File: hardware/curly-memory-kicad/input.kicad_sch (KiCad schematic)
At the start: 28 parts, among them J201 AudioJack2, J202 AudioJack2, J203 AudioJack2, J204 Conn_01x01_Male, J205 Conn_01x01_Male, J206 Conn_01x01_Male, J207 Conn_01x01_Male, U201 MCP6004

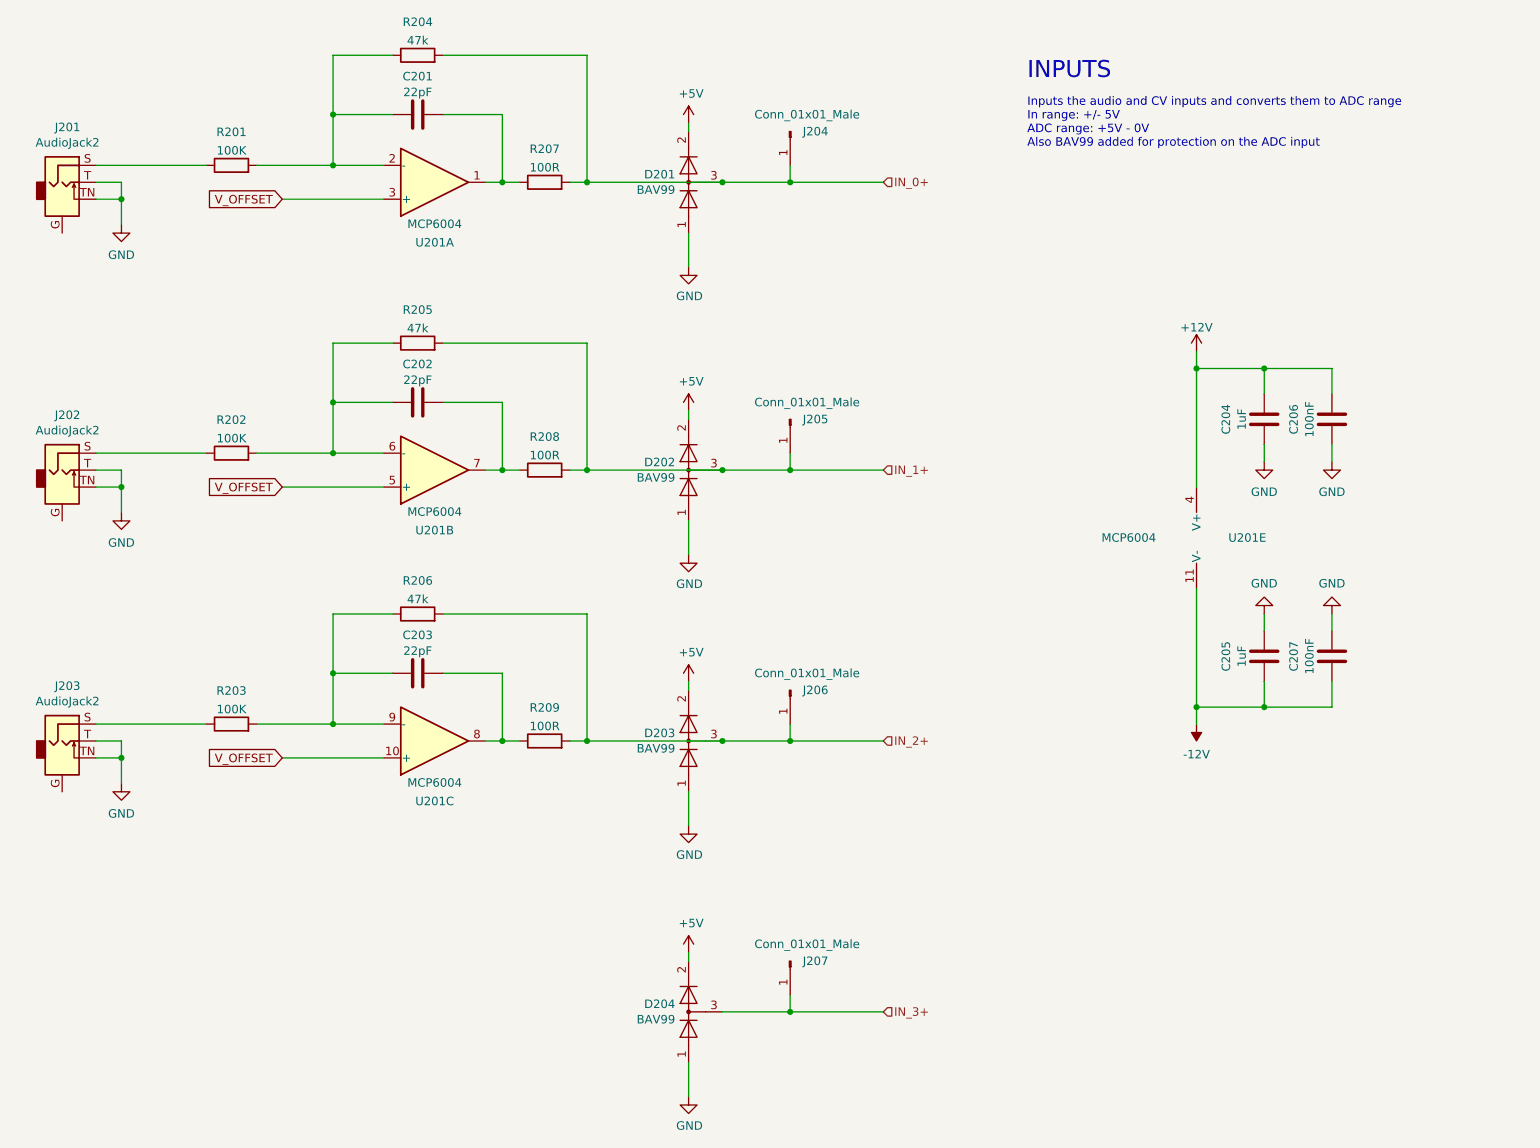
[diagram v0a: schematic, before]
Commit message: all components placed on the main board
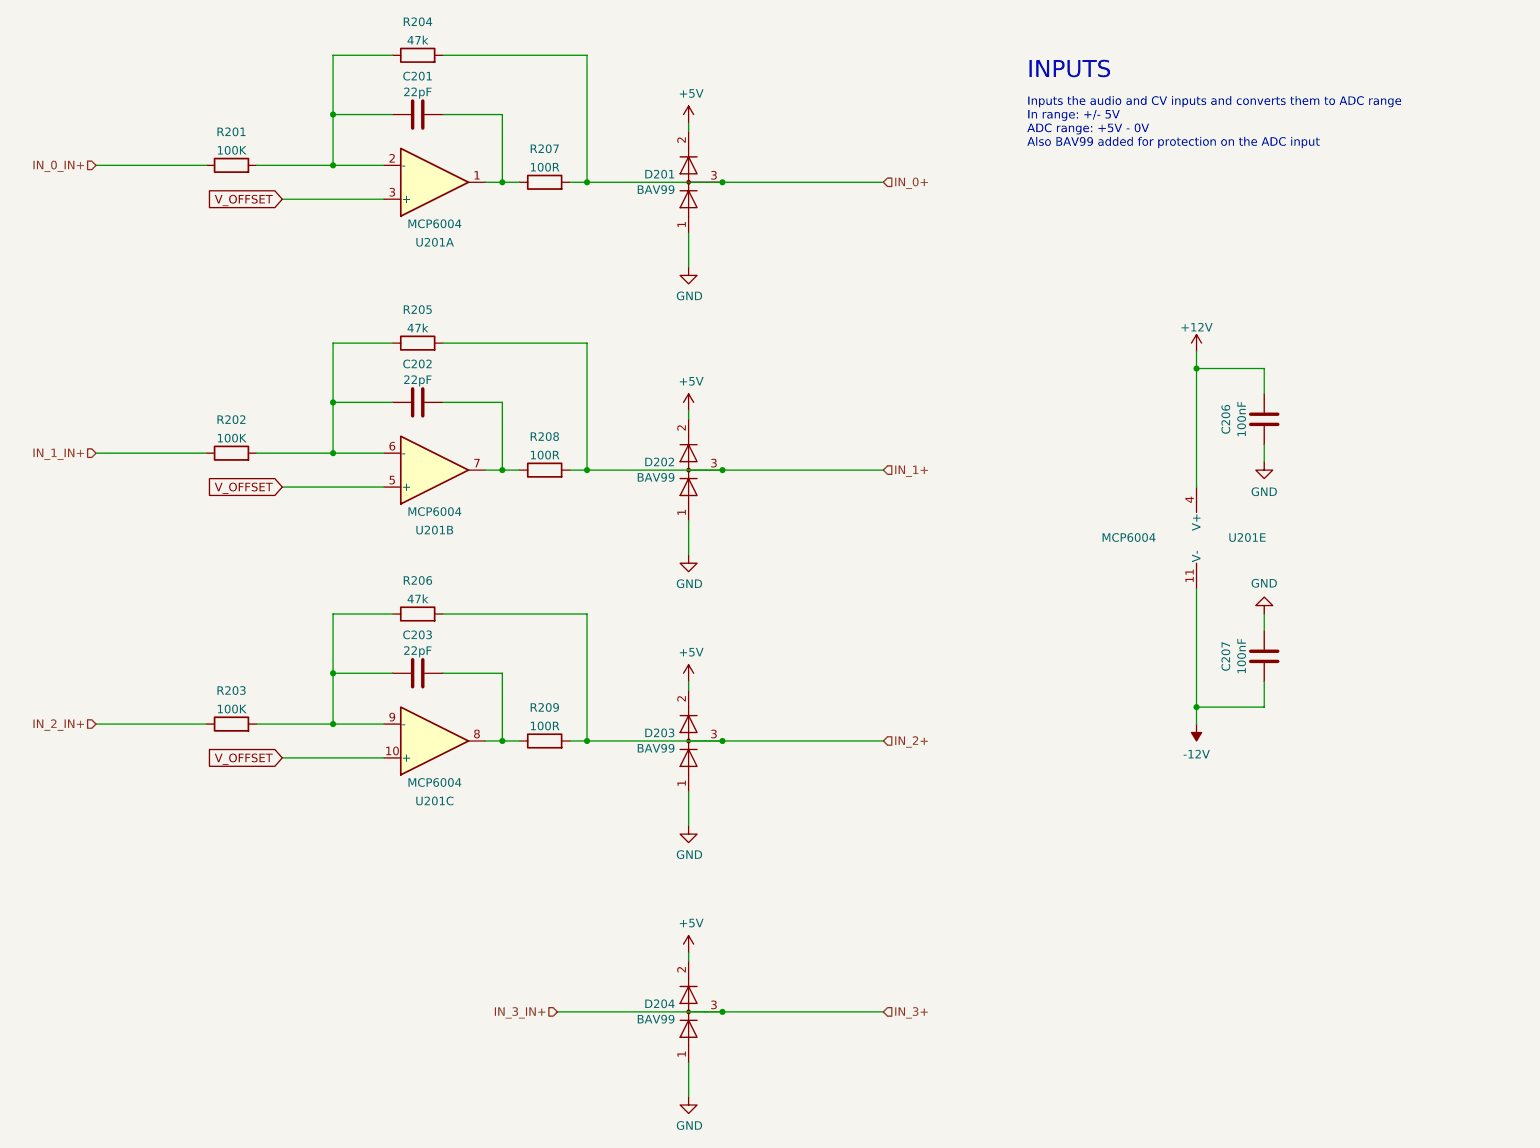
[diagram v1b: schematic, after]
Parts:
- removed C204, C205: 1uF, Capacitor_SMD:C_0805_2012Metric_Pad1.18x1.45mm_HandSolder, symbol Device:C
- removed J201, J202, J203: AudioJack2, AudioJacks:Jack_3.5mm_QingPu_WQP-PJ398SM_Vertical, symbol Connector:AudioJack2_Ground_SwitchT
- removed J204, J205, J206, J207: Conn_01x01_Male, Connector_PinSocket_2.54mm:PinSocket_1x01_P2.54mm_Vertical, symbol Connector:Conn_01x01_Male
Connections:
- net IN_0_IN+: now reaches R201.1
- net IN_1_IN+: now reaches R202.1
- net IN_2_IN+: now reaches R203.1
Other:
- moved on the sheet: C206, C207

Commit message: gerbers genearted and mf/mfpn added for main board for build
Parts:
- C201, C202, C203: MF (none) -> Samsung; MFPN (none) -> CL21C220JBANNNC; Material (none) -> CG0 / NP0; Voltage (none) -> 50V
- C206, C207: MF (none) -> Samsung; MFPN (none) -> CL21B104KBCNNNC; Material (none) -> X7R; Voltage (none) -> 50V
- R201, R202, R203: MF (none) -> Multicomp; MFPN (none) -> MCWR08X1003FTL; Tolerance (none) -> 1%
- R204, R205, R206: value 47k -> 47K; MF (none) -> Multicomp; MFPN (none) -> MCWR08X4702FTL; Tolerance (none) -> 1%
- R207, R208, R209: MF (none) -> Multicomp; MFPN (none) -> MCWR08X1000FTL; Tolerance (none) -> 1%
- U201: value MCP6004 -> MCP6004-I/SL
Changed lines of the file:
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@@
     (in_bom yes) (on_board yes) (fields_autoplaced)
     (property "Reference" "R206" (id 0) (at 81.28 100.4275 90))
-    (property "Value" "47k" (id 1) (at 81.28 103.2026 90))
+    (property "Value" "47K" (id 1) (at 81.28 103.2026 90))
     (property "Footprint" "Resistor_SMD:R_0805_2012Metric_Pad1.20x1.40mm_HandSolder" (id 2) (at 81.28 107.188 90)
       (effects (font (size 1.27 1.27)) hide)
     )
     (property "Datasheet" "~" (id 3) (at 81.28 105.41 0)
+      (effects (font (size 1.27 1.27)) hide)
+    )
+    (property "MF" "Multicomp" (id 4) (at 81.28 105.41 0)
+      (effects (font (size 1.27 1.27)) hide)
+    )
+    (property "MFPN" "MCWR08X4702FTL " (id 5) (at 81.28 105.41 0)
+      (effects (font (size 1.27 1.27)) hide)
+    )
+    (property "Tolerance" "1%" (id 6) (at 81.28 105.41 0)
       (effects (font (size 1.27 1.27)) hide)
     )
@@
       (effects (font (size 1.27 1.27)) hide)
     )
+    (property "Voltage" "50V" (id 4) (at 81.28 30.48 0)
+      (effects (font (size 1.27 1.27)) hide)
+    )
+    (property "MF" "Samsung" (id 5) (at 81.28 30.48 0)
+      (effects (font (size 1.27 1.27)) hide)
+    )
+    (property "MFPN" "CL21C220JBANNNC" (id 6) (at 81.28 30.48 0)
+      (effects (font (size 1.27 1.27)) hide)
+    )
+    (property "Material" "CG0 / NP0" (id 7) (at 81.28 30.48 0)
+      (effects (font (size 1.27 1.27)) hide)
+    )
     (pin "1")
     (pin "2")
@@
     (in_bom yes) (on_board yes) (fields_autoplaced)
     (property "Reference" "U201" (id 0) (at 83.82 49.6865 0))
-    (property "Value" "MCP6004" (id 1) (at 83.82 46.9114 0))
+    (property "Value" "MCP6004-I/SL" (id 1) (at 83.82 46.9114 0))
     (property "Footprint" "Package_SO:SOIC-14_3.9x8.7mm_P1.27mm" (id 2) (at 82.55 43.18 0)
       (effects (font (size 1.27 1.27)) hide)
@@
     (in_bom yes) (on_board yes) (fields_autoplaced)
     (property "Reference" "R205" (id 0) (at 81.28 59.7875 90))
-    (property "Value" "47k" (id 1) (at 81.28 62.5626 90))
+    (property "Value" "47K" (id 1) (at 81.28 62.5626 90))
     (property "Footprint" "Resistor_SMD:R_0805_2012Metric_Pad1.20x1.40mm_HandSolder" (id 2) (at 81.28 66.548 90)
       (effects (font (size 1.27 1.27)) hide)
     )
     (property "Datasheet" "~" (id 3) (at 81.28 64.77 0)
+      (effects (font (size 1.27 1.27)) hide)
+    )
+    (property "MF" "Multicomp" (id 4) (at 81.28 64.77 0)
+      (effects (font (size 1.27 1.27)) hide)
+    )
+    (property "MFPN" "MCWR08X4702FTL " (id 5) (at 81.28 64.77 0)
+      (effects (font (size 1.27 1.27)) hide)
+    )
+    (property "Tolerance" "1%" (id 6) (at 81.28 64.77 0)
       (effects (font (size 1.27 1.27)) hide)
     )
@@
       (effects (font (size 1.27 1.27)) hide)
     )
+    (property "Voltage" "50V" (id 4) (at 81.28 73.66 0)
+      (effects (font (size 1.27 1.27)) hide)
+    )
+    (property "MF" "Samsung" (id 5) (at 81.28 73.66 0)
+      (effects (font (size 1.27 1.27)) hide)
+    )
+    (property "MFPN" "CL21C220JBANNNC" (id 6) (at 81.28 73.66 0)
+      (effects (font (size 1.27 1.27)) hide)
+    )
+    (property "Material" "CG0 / NP0" (id 7) (at 81.28 73.66 0)
+      (effects (font (size 1.27 1.27)) hide)
+    )
     (pin "1")
     (pin "2")
@@
       (effects (font (size 1.27 1.27)) hide)
     )
+    (property "Voltage" "50V" (id 4) (at 208.28 111.76 0)
+      (effects (font (size 1.27 1.27)) hide)
+    )
+    (property "MF" "Samsung" (id 5) (at 208.28 111.76 0)
+      (effects (font (size 1.27 1.27)) hide)
+    )
+    (property "MFPN" "CL21B104KBCNNNC" (id 6) (at 208.28 111.76 0)
+      (effects (font (size 1.27 1.27)) hide)
+    )
+    (property "Material" "X7R" (id 7) (at 208.28 111.76 0)
+      (effects (font (size 1.27 1.27)) hide)
+    )
     (pin "1")
     (pin "2")
@@
       (effects (font (size 1.27 1.27)) hide)
     )
+    (property "MF" "Multicomp" (id 4) (at 100.33 124.46 0)
+      (effects (font (size 1.27 1.27)) hide)
+    )
+    (property "MFPN" "MCWR08X1000FTL " (id 5) (at 100.33 124.46 0)
+      (effects (font (size 1.27 1.27)) hide)
+    )
+    (property "Tolerance" "1%" (id 6) (at 100.33 124.46 0)
+      (effects (font (size 1.27 1.27)) hide)
+    )
     (pin "1")
     (pin "2")
@@
       (effects (font (size 1.27 1.27)) hide)
     )
+    (property "Voltage" "50V" (id 4) (at 81.28 114.3 0)
+      (effects (font (size 1.27 1.27)) hide)
+    )
+    (property "MF" "Samsung" (id 5) (at 81.28 114.3 0)
+      (effects (font (size 1.27 1.27)) hide)
+    )
+    (property "MFPN" "CL21C220JBANNNC" (id 6) (at 81.28 114.3 0)
+      (effects (font (size 1.27 1.27)) hide)
+    )
+    (property "Material" "CG0 / NP0" (id 7) (at 81.28 114.3 0)
+      (effects (font (size 1.27 1.27)) hide)
+    )
     (pin "1")
     (pin "2")
@@
       (effects (font (size 1.27 1.27)) hide)
     )
+    (property "MF" "Multicomp" (id 4) (at 100.33 40.64 0)
+      (effects (font (size 1.27 1.27)) hide)
+    )
+    (property "MFPN" "MCWR08X1000FTL " (id 5) (at 100.33 40.64 0)
+      (effects (font (size 1.27 1.27)) hide)
+    )
+    (property "Tolerance" "1%" (id 6) (at 100.33 40.64 0)
+      (effects (font (size 1.27 1.27)) hide)
+    )
     (pin "1")
     (pin "2")
@@
       (effects (font (size 1.27 1.27)) hide)
     )
+    (property "Voltage" "50V" (id 4) (at 208.28 76.2 0)
+      (effects (font (size 1.27 1.27)) hide)
+    )
+    (property "MF" "Samsung" (id 5) (at 208.28 76.2 0)
+      (effects (font (size 1.27 1.27)) hide)
+    )
+    (property "MFPN" "CL21B104KBCNNNC" (id 6) (at 208.28 76.2 0)
+      (effects (font (size 1.27 1.27)) hide)
+    )
+    (property "Material" "X7R" (id 7) (at 208.28 76.2 0)
+      (effects (font (size 1.27 1.27)) hide)
+    )
     (pin "1")
     (pin "2")
@@
     (in_bom yes) (on_board yes) (fields_autoplaced)
     (property "Reference" "R204" (id 0) (at 81.28 16.6075 90))
-    (property "Value" "47k" (id 1) (at 81.28 19.3826 90))
+    (property "Value" "47K" (id 1) (at 81.28 19.3826 90))
     (property "Footprint" "Resistor_SMD:R_0805_2012Metric_Pad1.20x1.40mm_HandSolder" (id 2) (at 81.28 23.368 90)
       (effects (font (size 1.27 1.27)) hide)
@@
       (effects (font (size 1.27 1.27)) hide)
     )
+    (property "MF" "Multicomp" (id 4) (at 81.28 21.59 0)
+      (effects (font (size 1.27 1.27)) hide)
+    )
+    (property "MFPN" "MCWR08X4702FTL " (id 5) (at 81.28 21.59 0)
+      (effects (font (size 1.27 1.27)) hide)
+    )
+    (property "Tolerance" "1%" (id 6) (at 81.28 21.59 0)
+      (effects (font (size 1.27 1.27)) hide)
+    )
     (pin "1")
     (pin "2")
@@
     (in_bom yes) (on_board yes) (fields_autoplaced)
     (property "Reference" "U201" (id 0) (at 83.82 133.5065 0))
-    (property "Value" "MCP6004" (id 1) (at 83.82 130.7314 0))
+    (property "Value" "MCP6004-I/SL" (id 1) (at 83.82 130.7314 0))
     (property "Footprint" "Package_SO:SOIC-14_3.9x8.7mm_P1.27mm" (id 2) (at 82.55 127 0)
       (effects (font (size 1.27 1.27)) hide)
@@
       (effects (font (size 1.27 1.27)) hide)
     )
+    (property "MF" "Multicomp" (id 4) (at 53.34 121.92 0)
+      (effects (font (size 1.27 1.27)) hide)
+    )
+    (property "MFPN" "MCWR08X1003FTL " (id 5) (at 53.34 121.92 0)
+      (effects (font (size 1.27 1.27)) hide)
+    )
+    (property "Tolerance" "1%" (id 6) (at 53.34 121.92 0)
+      (effects (font (size 1.27 1.27)) hide)
+    )
     (pin "1")
     (pin "2")
@@
     (in_bom yes) (on_board yes) (fields_autoplaced)
     (property "Reference" "U201" (id 0) (at 83.82 92.8665 0))
-    (property "Value" "MCP6004" (id 1) (at 83.82 90.0914 0))
+    (property "Value" "MCP6004-I/SL" (id 1) (at 83.82 90.0914 0))
     (property "Footprint" "Package_SO:SOIC-14_3.9x8.7mm_P1.27mm" (id 2) (at 82.55 86.36 0)
       (effects (font (size 1.27 1.27)) hide)
@@
       (effects (font (size 1.27 1.27)) hide)
     )
+    (property "MF" "Multicomp" (id 4) (at 100.33 83.82 0)
+      (effects (font (size 1.27 1.27)) hide)
+    )
+    (property "MFPN" "MCWR08X1000FTL " (id 5) (at 100.33 83.82 0)
+      (effects (font (size 1.27 1.27)) hide)
+    )
+    (property "Tolerance" "1%" (id 6) (at 100.33 83.82 0)
+      (effects (font (size 1.27 1.27)) hide)
+    )
     (pin "1")
     (pin "2")
@@
       (effects (font (size 1.27 1.27)) hide)
     )
+    (property "MF" "Multicomp" (id 4) (at 53.34 38.1 0)
+      (effects (font (size 1.27 1.27)) hide)
+    )
+    (property "MFPN" "MCWR08X1003FTL " (id 5) (at 53.34 38.1 0)
+      (effects (font (size 1.27 1.27)) hide)
+    )
+    (property "Tolerance" "1%" (id 6) (at 53.34 38.1 0)
+      (effects (font (size 1.27 1.27)) hide)
+    )
     (pin "1")
     (pin "2")
@@
     (in_bom yes) (on_board yes)
     (property "Reference" "U201" (id 0) (at 205.74 93.98 0))
-    (property "Value" "MCP6004" (id 1) (at 187.96 93.98 0))
+    (property "Value" "MCP6004-I/SL" (id 1) (at 187.96 93.98 0))
     (property "Footprint" "Package_SO:SOIC-14_3.9x8.7mm_P1.27mm" (id 2) (at 196.85 91.44 0)
       (effects (font (size 1.27 1.27)) hide)
@@
       (effects (font (size 1.27 1.27)) hide)
     )
+    (property "MF" "Multicomp" (id 4) (at 53.34 81.28 0)
+      (effects (font (size 1.27 1.27)) hide)
+    )
+    (property "MFPN" "MCWR08X1003FTL " (id 5) (at 53.34 81.28 0)
+      (effects (font (size 1.27 1.27)) hide)
+    )
+    (property "Tolerance" "1%" (id 6) (at 53.34 81.28 0)
+      (effects (font (size 1.27 1.27)) hide)
+    )
